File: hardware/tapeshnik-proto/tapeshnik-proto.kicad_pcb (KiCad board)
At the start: 2 copper layers, 76.2 x 61 mm, 52 parts, among them J1 Conn_01x02, J2 RW_HEAD, J3 Conn_01x07, J4 ERASERHEAD, Q1 RFP30N06LE, Q2 S8050, Q3 S8550, Q4 S8050, U1 Pico, U2 74HC14, U3 CD4052B, U4 LM358, U5 LM358

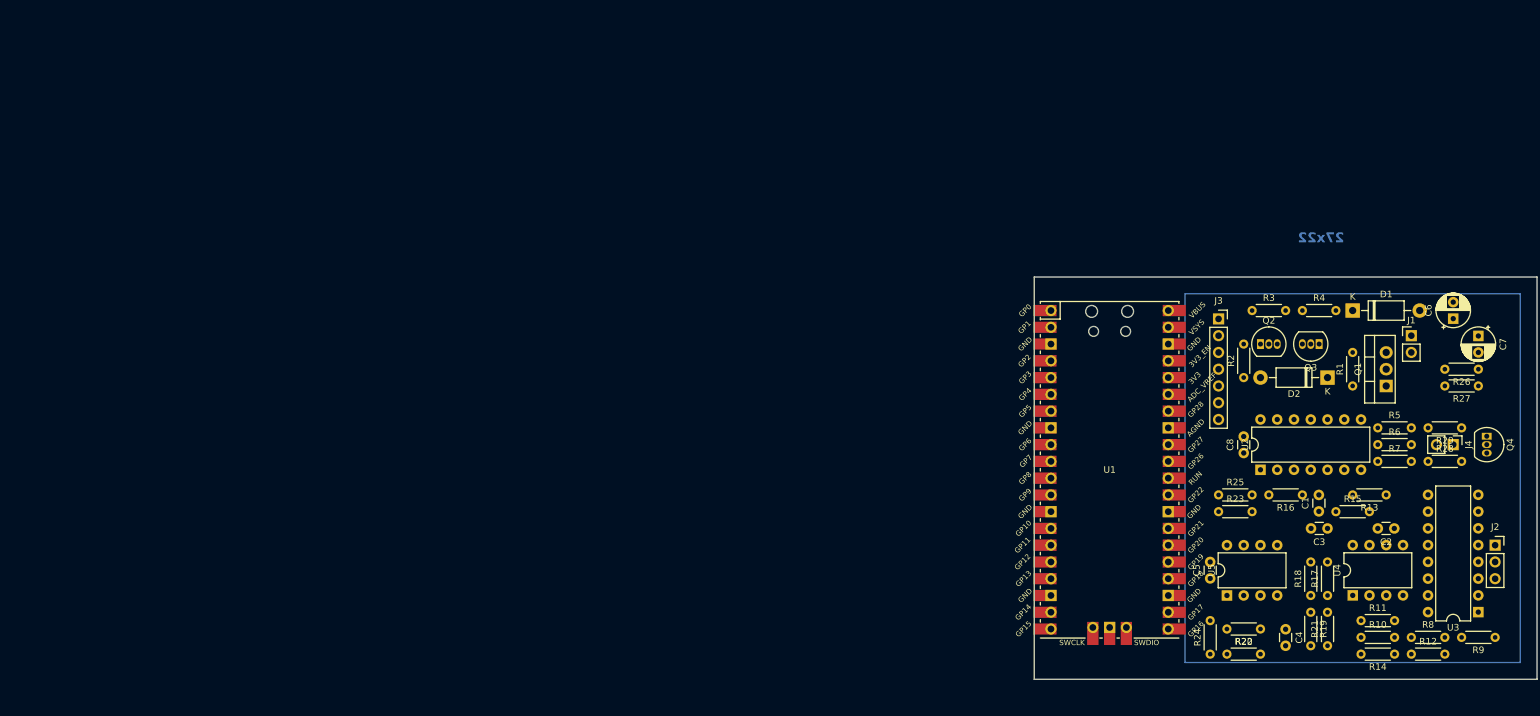
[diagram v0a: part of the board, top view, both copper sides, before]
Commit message: tape sector overwrite experiment in progress
pipico ded, working on the new pcb instead
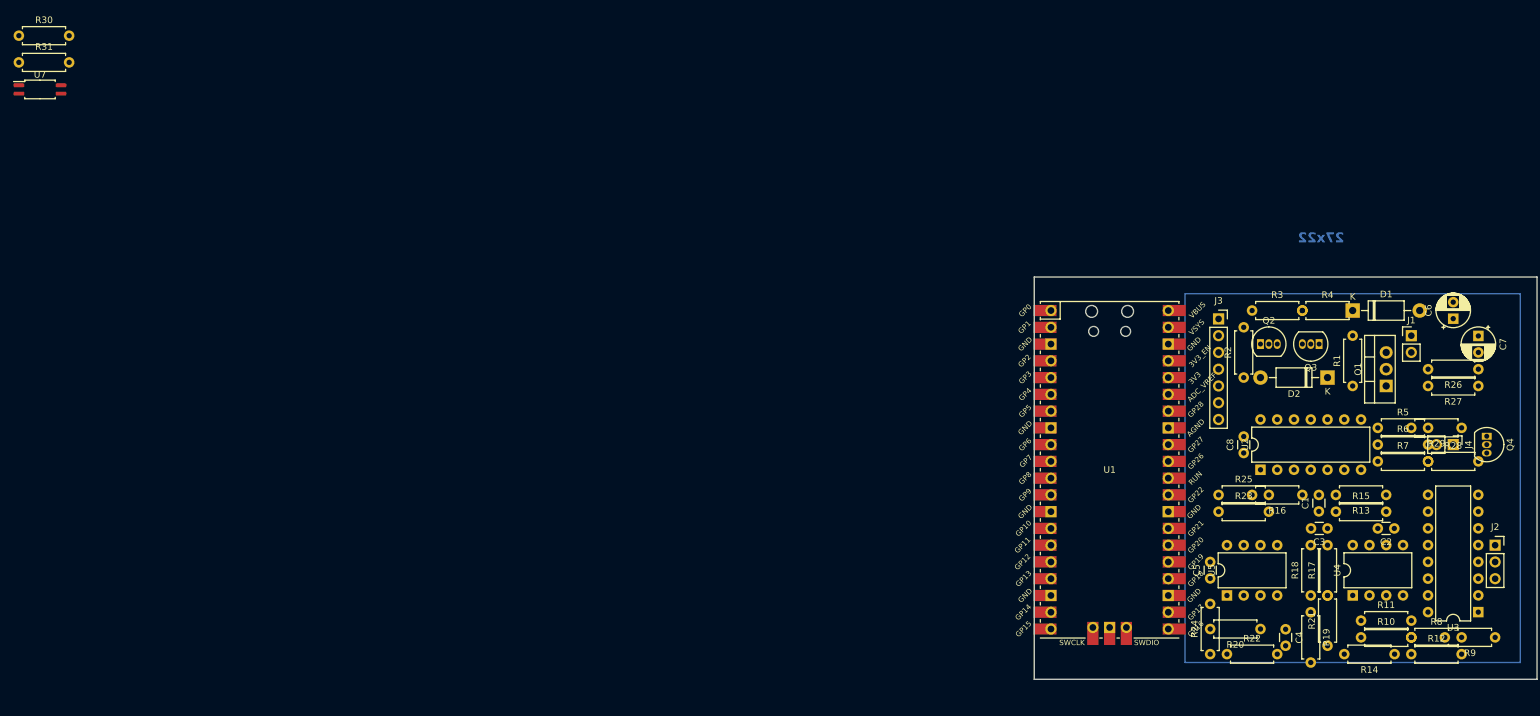
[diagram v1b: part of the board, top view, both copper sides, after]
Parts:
- added R30: 47, Resistor_THT:R_Axial_DIN0207_L6.3mm_D2.5mm_P7.62mm_Horizontal, F.Cu at (1.07, 1.52)
- added R31: 10K, Resistor_THT:R_Axial_DIN0207_L6.3mm_D2.5mm_P7.62mm_Horizontal, F.Cu at (1.07, 5.58)
- added U7: TCRT1000, Package_SO:SOP-4_4.4x2.6mm_P1.27mm, F.Cu at (4.28, 9.68)
- R1, R10, R11, R12, R13, R14, R15, R16, R17, R18, R19, R2, R20, R21, R22, R23, R24, R25, R26, R27, R28, R29, R3, R4, R5, R6, R7, R8, R9: footprint Resistor_THT:R_Axial_DIN0204_L3.6mm_D1.6mm_P5.08mm_Horizontal -> Resistor_THT:R_Axial_DIN0207_L6.3mm_D2.5mm_P7.62mm_Horizontal
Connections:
- J3 pad 5: /CAS_INT -> /CAS_TACHO
- U1 pad 25: unconnected-(U1-GPIO19-Pad25) -> /CAS_TACHO
- U1 pad 36: unconnected-(U1-3V3-Pad36) -> +3V3
